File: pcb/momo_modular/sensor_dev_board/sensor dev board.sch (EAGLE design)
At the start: 9 parts

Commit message: Corrected connections for PG lines
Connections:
- removed net N$4: JP2.5, U$1.3, U$2.RA1/PCLK/CLK
- new net N$8: JP1.5, JP2.5, U$1.3, U$2.RA1/PCLK/CLK
- net N$7: no longer JP1.5
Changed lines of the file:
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@@
-</segment>
-</net>
-<net name="N$4" class="0">
-<segment>
-<pinref part="JP2" gate="A" pin="5"/>
-<wire x1="147.32" y1="55.88" x2="132.08" y2="55.88" width="0.1524" layer="91"/>
-<wire x1="132.08" y1="55.88" x2="132.08" y2="53.34" width="0.1524" layer="91"/>
-<pinref part="U$2" gate="G$1" pin="RA1/PCLK/CLK"/>
-<wire x1="132.08" y1="53.34" x2="106.68" y2="53.34" width="0.1524" layer="91"/>
-<pinref part="U$1" gate="G$1" pin="3"/>
-<wire x1="106.68" y1="53.34" x2="88.9" y2="53.34" width="0.1524" layer="91"/>
-<wire x1="106.68" y1="88.9" x2="106.68" y2="53.34" width="0.1524" layer="91"/>
-<junction x="106.68" y="53.34"/>
 </segment>
 </net>
@@
 <wire x1="139.7" y1="45.72" x2="139.7" y2="48.26" width="0.1524" layer="91"/>
 <pinref part="U$2" gate="G$1" pin="RA5"/>
-<wire x1="88.9" y1="45.72" x2="104.14" y2="45.72" width="0.1524" layer="91"/>
-<pinref part="JP1" gate="A" pin="5"/>
-<wire x1="104.14" y1="45.72" x2="111.76" y2="45.72" width="0.1524" layer="91"/>
+<wire x1="88.9" y1="45.72" x2="111.76" y2="45.72" width="0.1524" layer="91"/>
 <wire x1="111.76" y1="45.72" x2="139.7" y2="45.72" width="0.1524" layer="91"/>
-<wire x1="63.5" y1="93.98" x2="63.5" y2="71.12" width="0.1524" layer="91"/>
-<wire x1="63.5" y1="71.12" x2="104.14" y2="71.12" width="0.1524" layer="91"/>
-<wire x1="104.14" y1="71.12" x2="104.14" y2="45.72" width="0.1524" layer="91"/>
-<junction x="104.14" y="45.72"/>
 <pinref part="U$1" gate="G$1" pin="5"/>
 <wire x1="111.76" y1="88.9" x2="111.76" y2="45.72" width="0.1524" layer="91"/>
@@
 </segment>
 </net>
+<net name="N$8" class="0">
+<segment>
+<pinref part="JP1" gate="A" pin="5"/>
+<wire x1="63.5" y1="93.98" x2="63.5" y2="71.12" width="0.1524" layer="91"/>
+<wire x1="63.5" y1="71.12" x2="106.68" y2="71.12" width="0.1524" layer="91"/>
+<pinref part="JP2" gate="A" pin="5"/>
+<wire x1="147.32" y1="55.88" x2="132.08" y2="55.88" width="0.1524" layer="91"/>
+<wire x1="132.08" y1="55.88" x2="132.08" y2="53.34" width="0.1524" layer="91"/>
+<pinref part="U$2" gate="G$1" pin="RA1/PCLK/CLK"/>
+<wire x1="132.08" y1="53.34" x2="106.68" y2="53.34" width="0.1524" layer="91"/>
+<pinref part="U$1" gate="G$1" pin="3"/>
+<wire x1="106.68" y1="53.34" x2="88.9" y2="53.34" width="0.1524" layer="91"/>
+<wire x1="106.68" y1="88.9" x2="106.68" y2="71.12" width="0.1524" layer="91"/>
+<junction x="106.68" y="53.34"/>
+<wire x1="106.68" y1="71.12" x2="106.68" y2="53.34" width="0.1524" layer="91"/>
+<junction x="106.68" y="71.12"/>
+</segment>
+</net>

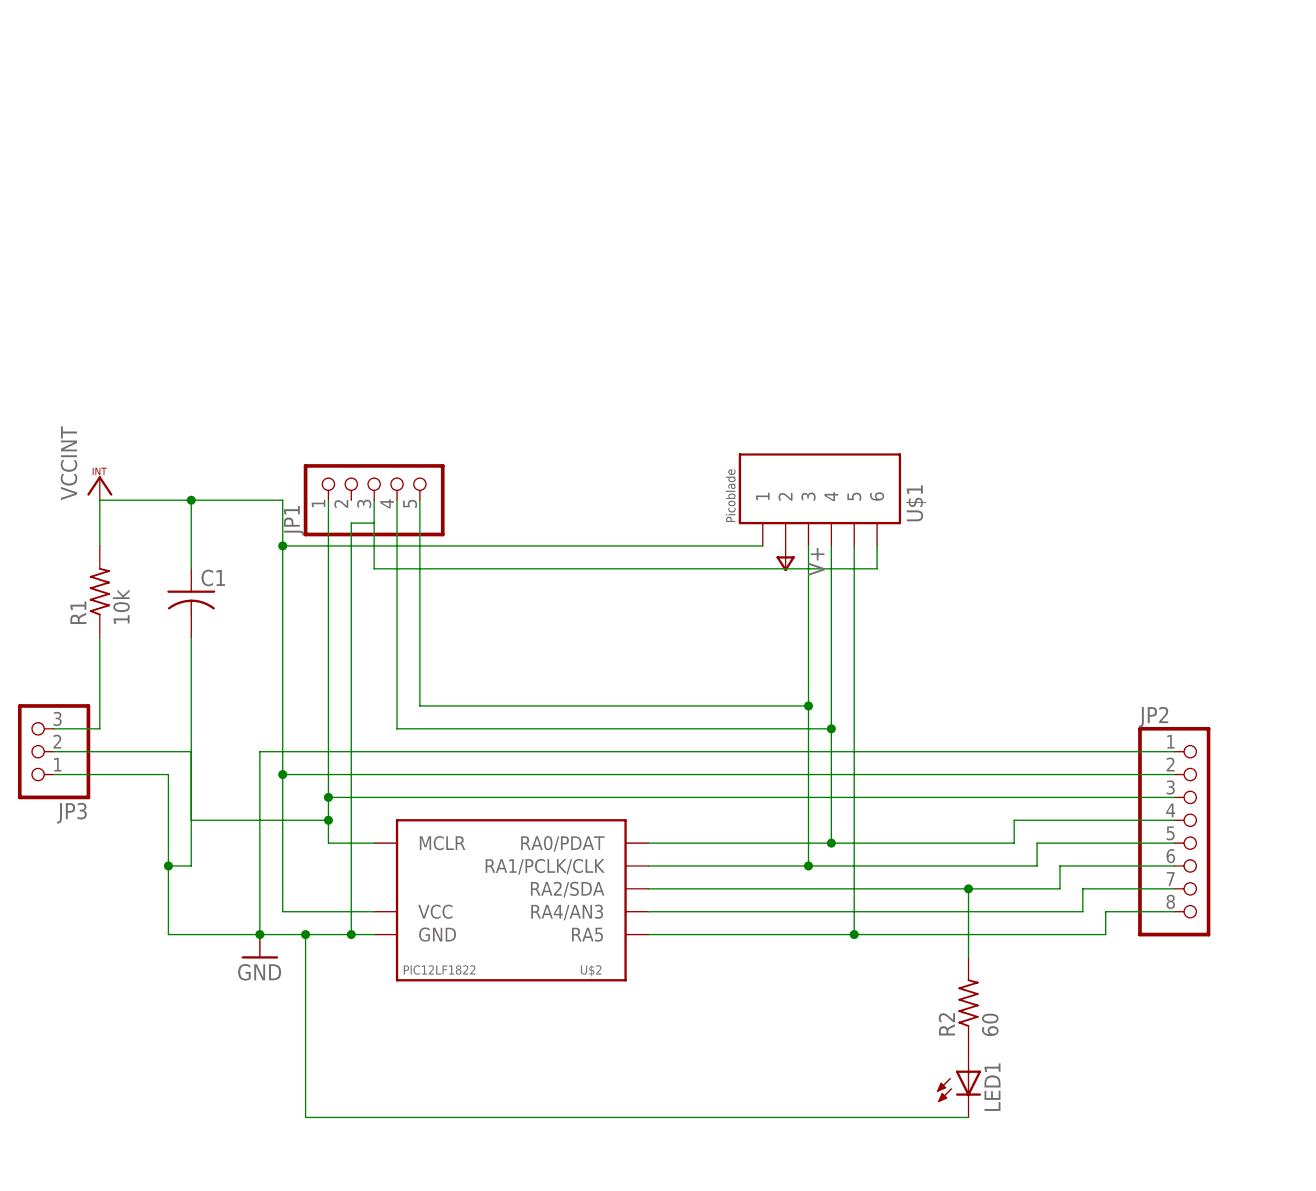
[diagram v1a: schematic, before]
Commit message: Changed I2C Data line and added second indicator LED on 2.8V line
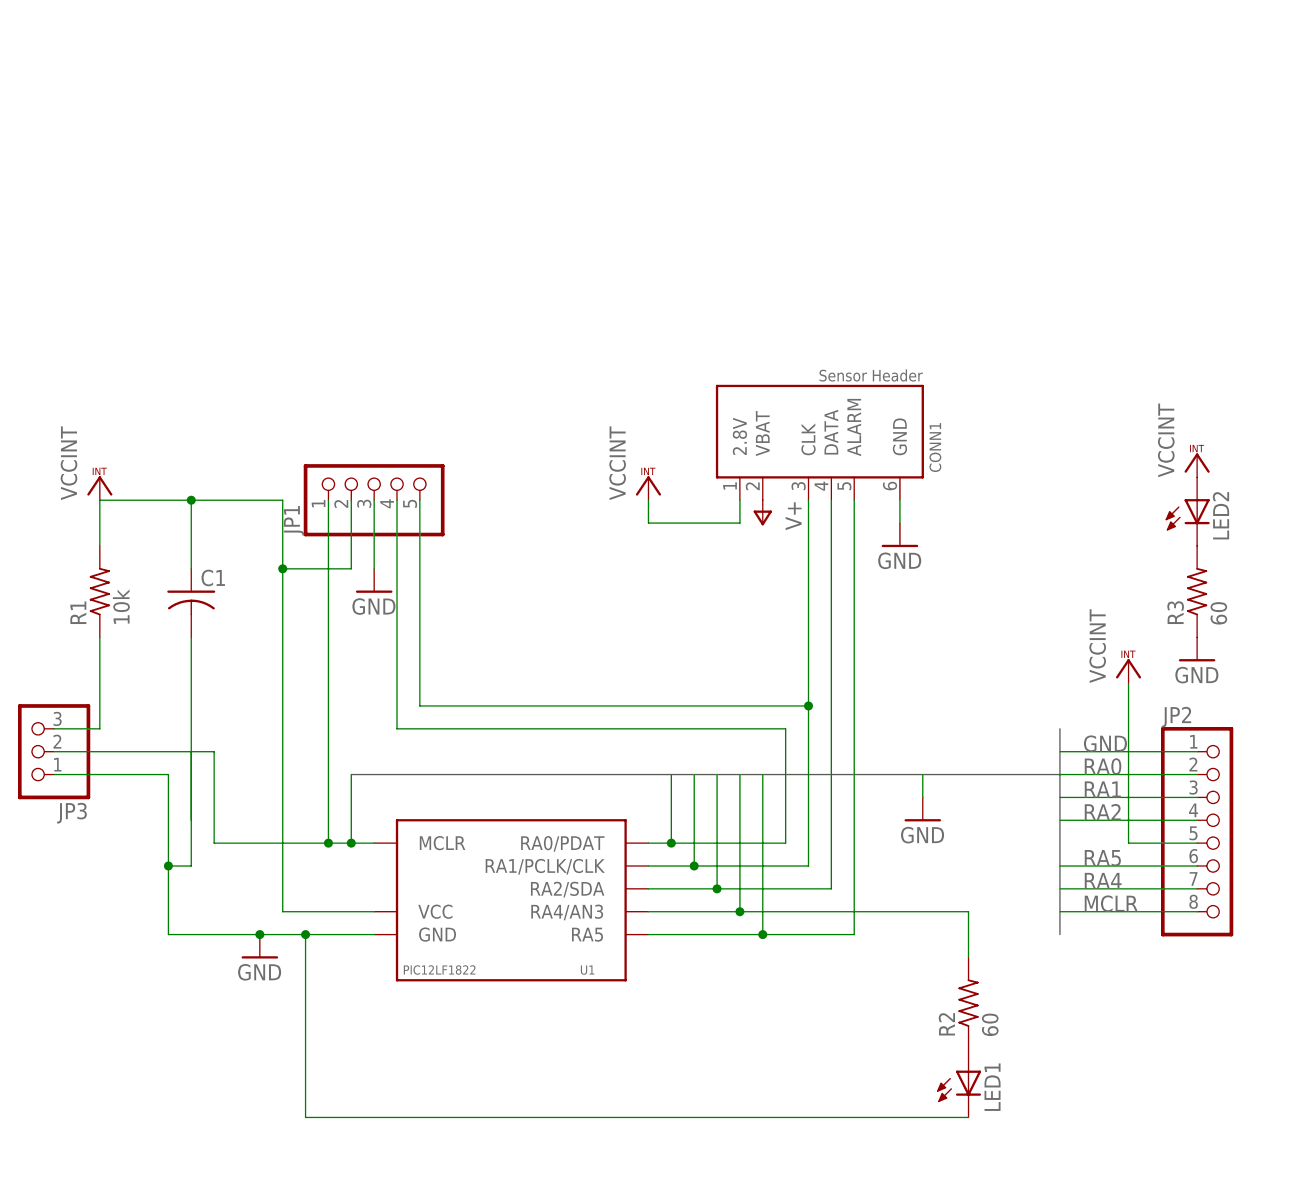
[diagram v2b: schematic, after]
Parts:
- removed U$1: 2X3-MOLEX-90130, components:2X3-MOLEX-90130
- added CONN1: MOMO-SENSOR-HEADER, components:MOMO-SENSOR-HEADER
- added LED2: (no value), led:LEDSML0603
- added R3: 60, resistor:R-US_R0603
- renumbered U$2 to U1
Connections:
- removed net N$3: JP2.6, R2.2, U1.RA2/SDA
- removed net N$5: JP1.4, JP2.4, U$1.4, U1.RA0/PDAT
- removed net N$6: JP1.1, JP2.3, JP3.2, U1.MCLR
- removed net N$7: JP2.8, U$1.5, U1.RA5
- removed net N$8: JP1.5, JP2.5, U$1.3, U1.RA1/PCLK/CLK
- new net MCLR: JP1.1, JP2.8, JP3.2, U1.MCLR
- new net RA0: JP1.4, JP2.2, U1.RA0/PDAT
- new net RA1: CONN1.CLK, JP1.5, JP2.3, U1.RA1/PCLK/CLK
- new net RA2: CONN1.DATA, JP2.4, U1.RA2/SDA
- new net RA4: JP2.7, R2.2, U1.RA4/AN3
- new net RA5: CONN1.ALARM, JP2.6, U1.RA5
- net GND: now also R3.1; no longer U$1.6
- net N$2: now also LED2.C, R3.2; no longer JP2.7, U1.RA4/AN3
- net V+: now also CONN1.VBAT; no longer U$1.2
- net VCCINT: now also CONN1.2.8V, JP1.2, JP2.5, LED2.A; no longer JP2.2, U$1.1
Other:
- moved on the sheet: JP2

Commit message: Sensor Dev Board Touches
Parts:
- C1: value (none) -> 100 nF
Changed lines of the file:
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@@
 <part name="R1" library="rcl" deviceset="R-US_" device="R0603" value="10k"/>
 <part name="P+1" library="supply1" deviceset="V+" device=""/>
-<part name="C1" library="rcl" deviceset="C-US" device="C0402"/>
+<part name="C1" library="rcl" deviceset="C-US" device="C0402" value="100 nF"/>
 <part name="R2" library="resistor" deviceset="R-US_" device="R0603" value="60"/>
 <part name="LED1" library="led" deviceset="LED" device="SML0603"/>

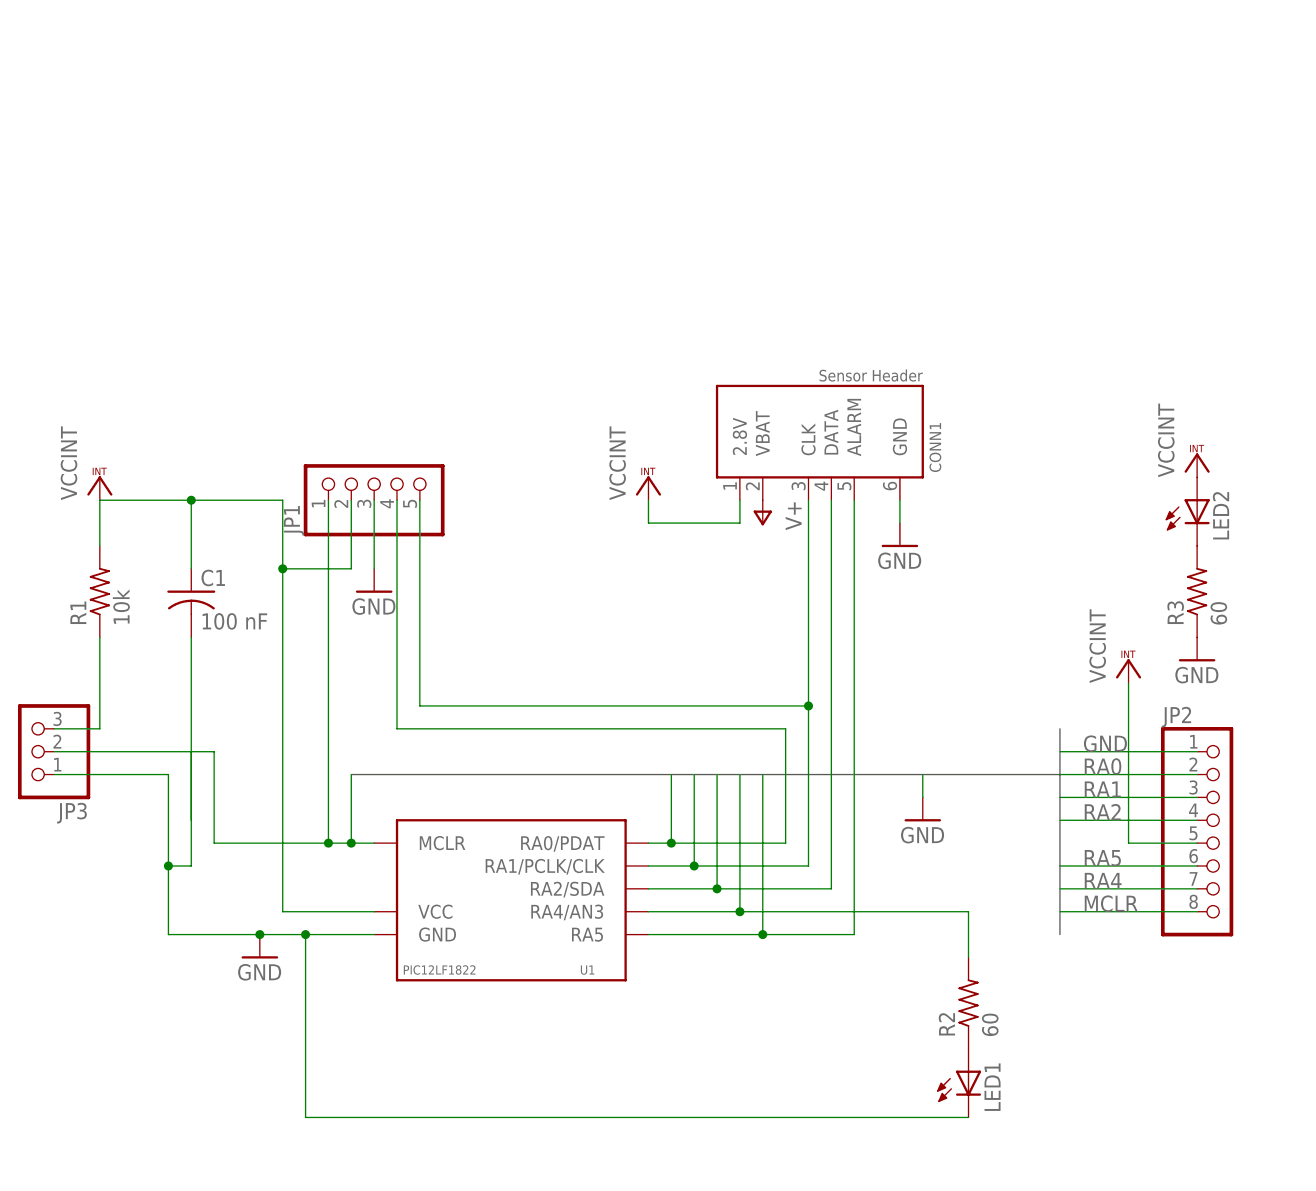
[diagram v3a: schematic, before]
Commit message: Finished next version of hardware.  Working on automatic BOM generation for purchasing.
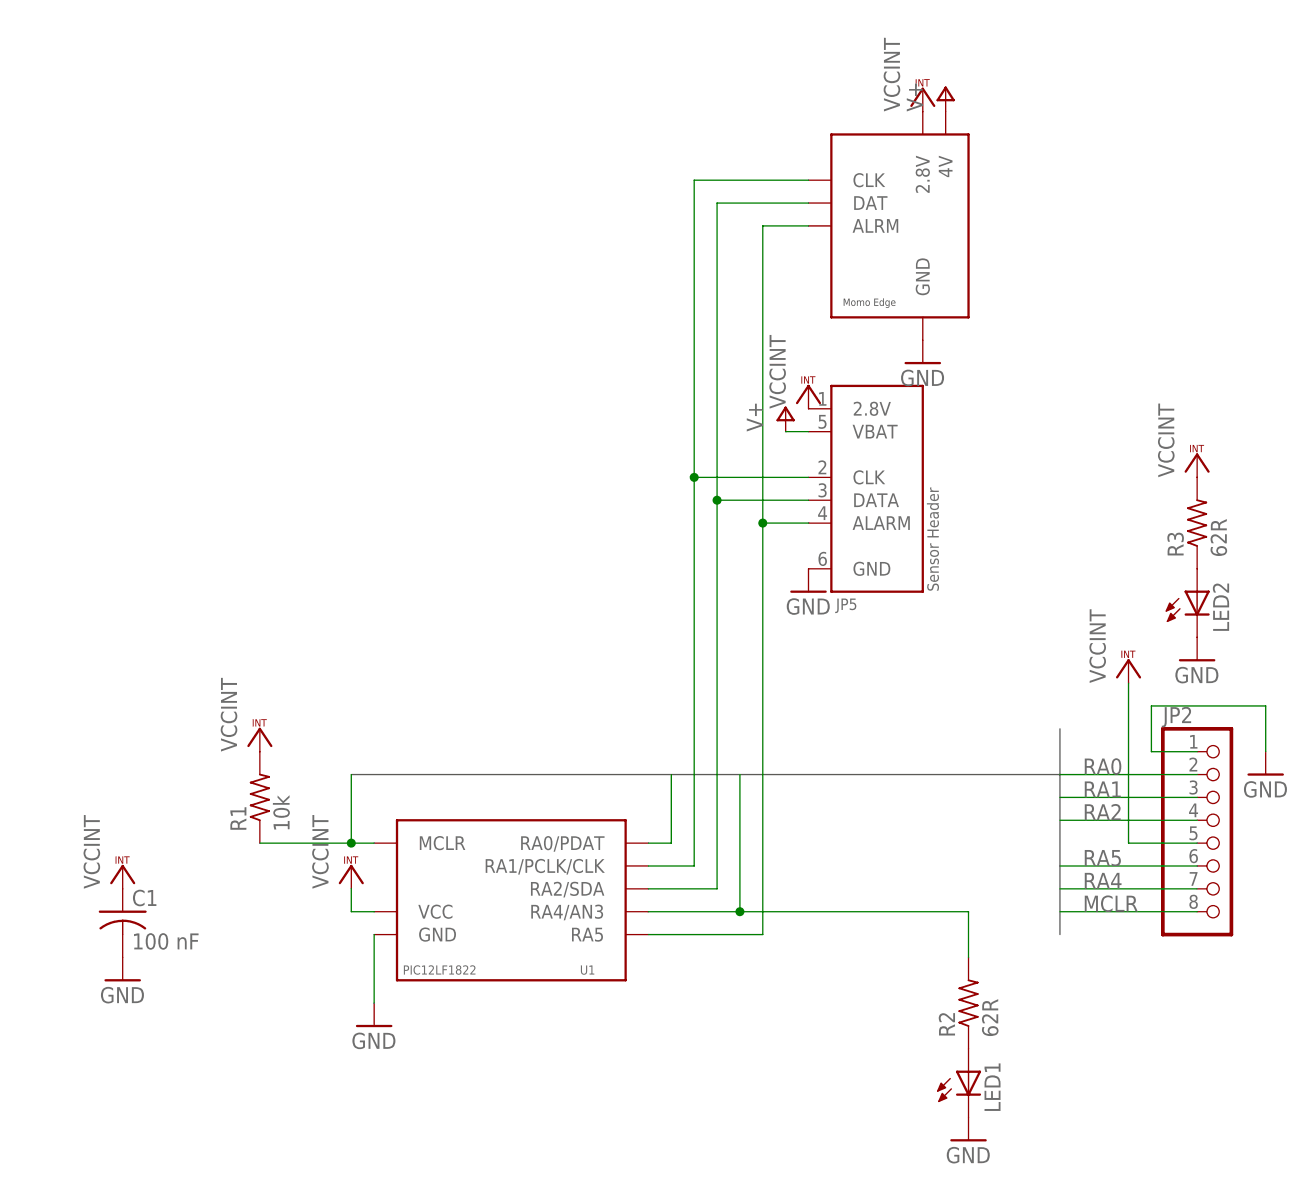
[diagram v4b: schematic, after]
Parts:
- removed CONN1: MOMO-SENSOR-HEADER, components:MOMO-SENSOR-HEADER
- removed JP1: (no value), pinhead:PINHD-1X5
- removed JP3: (no value), pinhead:PINHD-1X3
- added JP4: MOMO-VERT-6M, components:MOMO-VERT-6M
- added JP5: MOMO-SENSOR-RJ11, components:MOMO-SENSOR-RJ11
- C1: DIGIKEY-PN (none) -> 445-1265-1-ND
- JP2: DIGIKEY-PN (none) -> S1012EC-08-ND
- LED1, LED2: device led:LEDSML0603 -> led:LEDCHIP-LED0603; DIGIKEY-PN (none) -> 475-2709-1-ND
- R1: DIGIKEY-PN (none) -> P10.0KHCT-ND
- R2, R3: value 60 -> 62R; DIGIKEY-PN (none) -> P62GCT-ND
- U1: DIGIKEY-PN (none) -> PIC12LF1822-I/SN
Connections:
- removed net N$10: JP3.3, R1.1
- net GND: now also JP4.GND, JP5.GND, LED2.C; no longer JP1.3, JP3.1, R3.1
- net MCLR: now also R1.1; no longer JP1.1, JP3.2
- net N$2: now also LED2.A, R3.1; no longer LED2.C, R3.2
- net RA0: no longer JP1.4
- net RA1: now also JP4.CLK, JP5.CLK; no longer CONN1.CLK, JP1.5
- net RA2: now also JP4.DAT, JP5.DATA; no longer CONN1.DATA
- net RA5: now also JP4.ALRM, JP5.ALARM; no longer CONN1.ALARM
- net V+: now also JP4.4V, JP5.VBAT; no longer CONN1.VBAT
- net VCCINT: now also JP4.2.8V, JP5.2.8V, R3.2; no longer CONN1.2.8V, JP1.2, LED2.A
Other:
- moved on the sheet: C1, LED2, R1, R3
